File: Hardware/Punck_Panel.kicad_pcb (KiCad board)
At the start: 2 copper layers, 91.2 x 128.5 mm, 37 parts, among them J11 USB_B_Micro

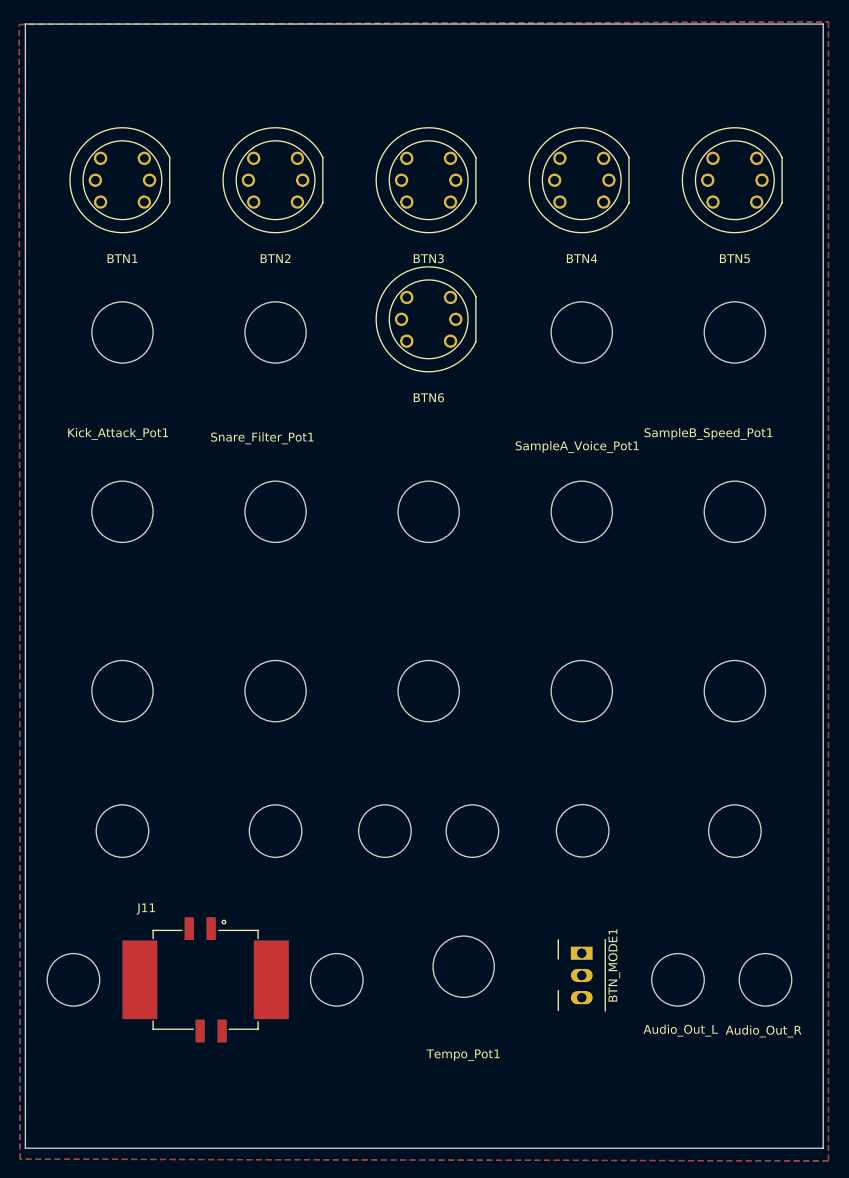
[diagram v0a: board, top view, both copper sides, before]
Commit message: Updated components on panel board
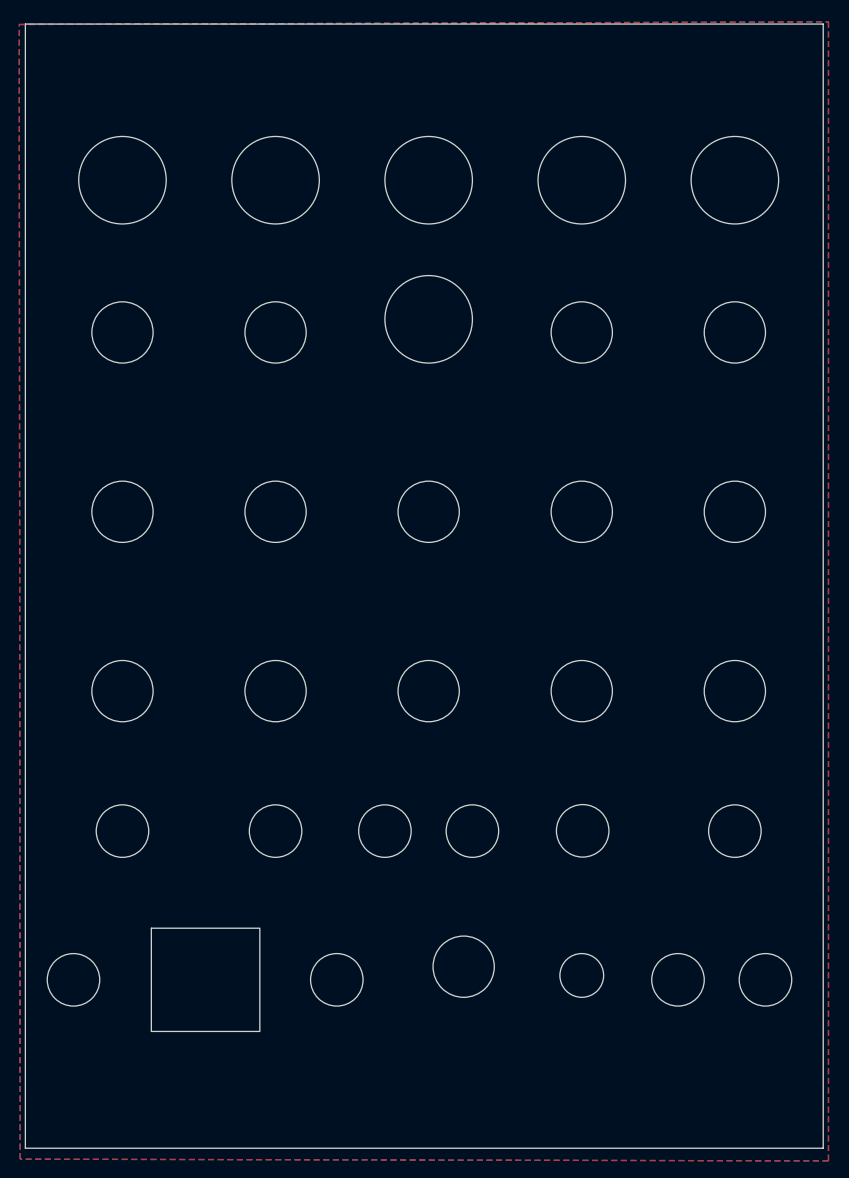
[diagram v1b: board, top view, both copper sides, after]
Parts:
- removed BTN1, BTN2, BTN3, BTN4, BTN5, BTN6: KS01-BLV, Custom_Footprints:KS01-BLV
- removed BTN_MODE1: SW_SPDT_MSM, Custom_Footprints:SPDT_SubMiniature_Aligned
- removed J11: USB_B_Micro, Custom_Footprints:USB_TE_1734517-1
- added Ref**: LED_Buttons_KS01-BLV, Custom_Footprints:LED_Buttons_KS01-BLV, F.Cu at (81.0, 58.6)
- added Ref**: LED_Buttons_KS01-BLV, Custom_Footprints:LED_Buttons_KS01-BLV, F.Cu at (116.0, 58.6)
- added Ref**: LED_Buttons_KS01-BLV, Custom_Footprints:LED_Buttons_KS01-BLV, F.Cu at (151.0, 58.6)
- added Ref**: LED_Buttons_KS01-BLV, Custom_Footprints:LED_Buttons_KS01-BLV, F.Cu at (133.5, 58.6)
- added Ref**: LED_Buttons_KS01-BLV, Custom_Footprints:LED_Buttons_KS01-BLV, F.Cu at (98.5, 58.6)
- added Ref**: LED_Buttons_KS01-BLV, Custom_Footprints:LED_Buttons_KS01-BLV, F.Cu at (116.0, 74.5)
- added Ref**: Subminiature_Switch, Custom_Footprints:Sub_Miniature_Switch_MountingHole_5mm, F.Cu at (133.5, 149.5)
- added USB**: USB_B_CUTOUT, Custom_Footprints:USB_B_CUTOUT, F.Cu at (90.5, 150.0)
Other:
- board text added: "Hi Hat Decay"
- board text added: "Hi Hat Level"
- board text added: "Kick Attack"
- board text added: "Kick Decay"
- board text added: "Kick Level"
- board text added: "MIDI In"
- board text added: "Out L"
- board text added: "Out R"
- board text added: "Sample A Level"
- board text added: "Sample A Speed"
- board text added: "Sample A Voice"
- board text added: "Sample B Level"
- board text added: "Sample B Speed"
- board text added: "Snare Filter"
- board text added: "Snare Level"
- board text added: "Snare Tuning"
- board text added: "Tempo"
- board text added: "Tempo Out"
- board text removed: "Audio_Out_L"
- board text removed: "Audio_Out_R"
- board text removed: "Kick_Attack_Pot1"
- board text removed: "SampleA_Voice_Pot1"
- board text removed: "SampleB_Speed_Pot1"
- board text removed: "Snare_Filter_Pot1"
- board text removed: "Tempo_Pot1"

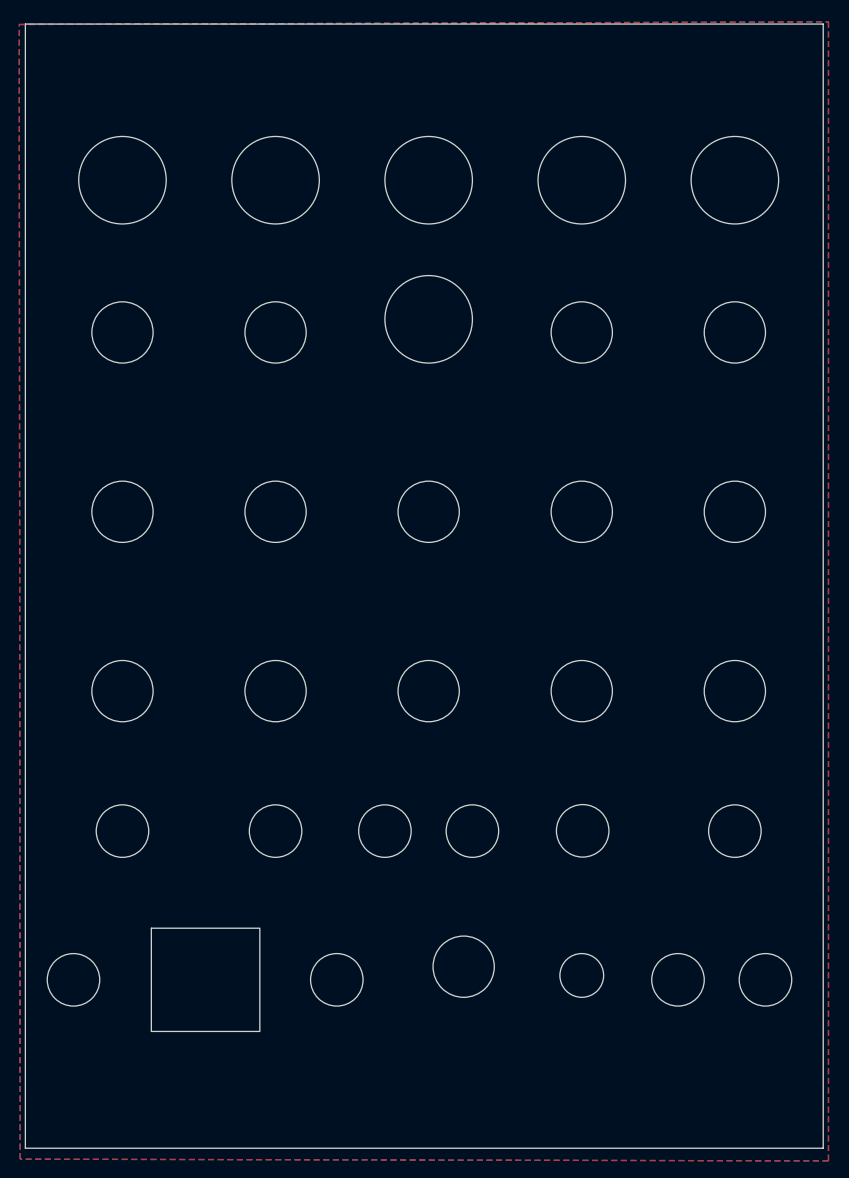
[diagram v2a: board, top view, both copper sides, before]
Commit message: Redesign of panel layout
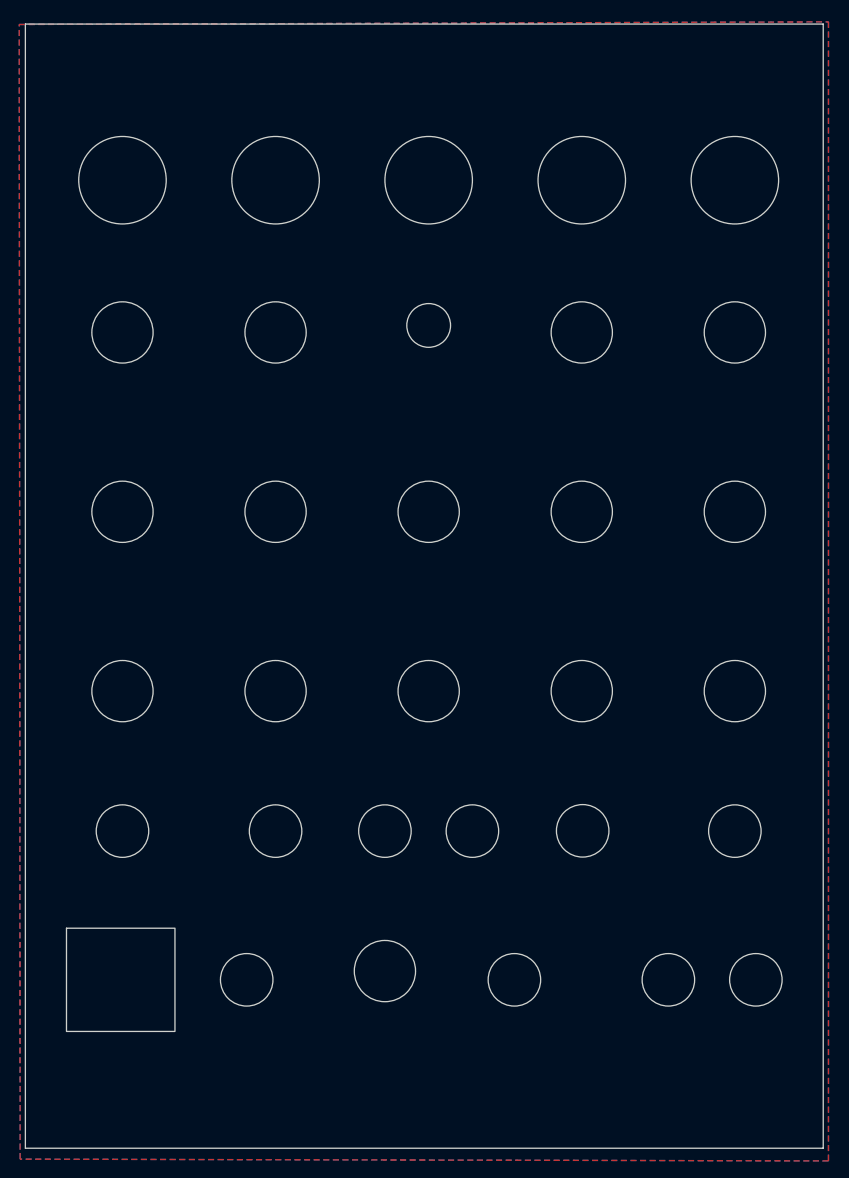
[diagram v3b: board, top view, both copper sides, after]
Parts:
- removed the Ref** at (116.0, 74.5)
- added kibuzzard-633EE0D0: G***, kibuzzard-633EE0D0, F.Cu at (81.2, 50.0)
- added kibuzzard-633EE0FA: G***, kibuzzard-633EE0FA, F.Cu at (98.6, 50.0)
- added kibuzzard-633EE108: G***, kibuzzard-633EE108, F.Cu at (116.2, 50.0)
- added kibuzzard-633EE168: G***, kibuzzard-633EE168, F.Cu at (141.8, 50.0)
- moved Ref** 76.3 mm to (116.0, 75.2)
- moved Ref** 20.3 mm to (125.8, 150.0)
- moved Ref** 19.8 mm to (95.2, 150.0)
- moved USB** 9.70 mm to (80.8, 150.0)
- moved Ref** 9.01 mm to (111.0, 149.0)
- moved Ref** 1.10 mm to (153.4, 150.0)
- moved Ref** 1.10 mm to (143.4, 150.0)
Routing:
- added copper zone on B.Cu, net (none)
- added copper zone on F.Cu, net (none)
- removed copper zone on B.Cu, net GND
- removed copper zone on F.Cu, net GND
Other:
- board text added: "Attack"
- board text added: "C"
- board text added: "Decay"
- board text added: "Filter"
- board text added: "IN"
- board text added: "L Out R"
- board text added: "Level"
- board text added: "MIDI"
- board text added: "MIDI Learn"
- board text added: "O"
- board text added: "Out"
- board text added: "Sequence"
- board text added: "Speed"
- board text added: "Tuning"
- board text added: "Voice"
- board text removed: "Hi Hat Decay"
- board text removed: "Hi Hat Level"
- board text removed: "Kick Attack"
- board text removed: "Kick Decay"
- board text removed: "Kick Level"
- board text removed: "MIDI In"
- board text removed: "Out L"
- board text removed: "Out R"
- board text removed: "Sample A Level"
- board text removed: "Sample A Speed"
- board text removed: "Sample A Voice"
- board text removed: "Sample B Level"
- board text removed: "Sample B Speed"
- board text removed: "Snare Filter"
- board text removed: "Snare Level"
- board text removed: "Snare Tuning"
- board text removed: "Tempo Out"

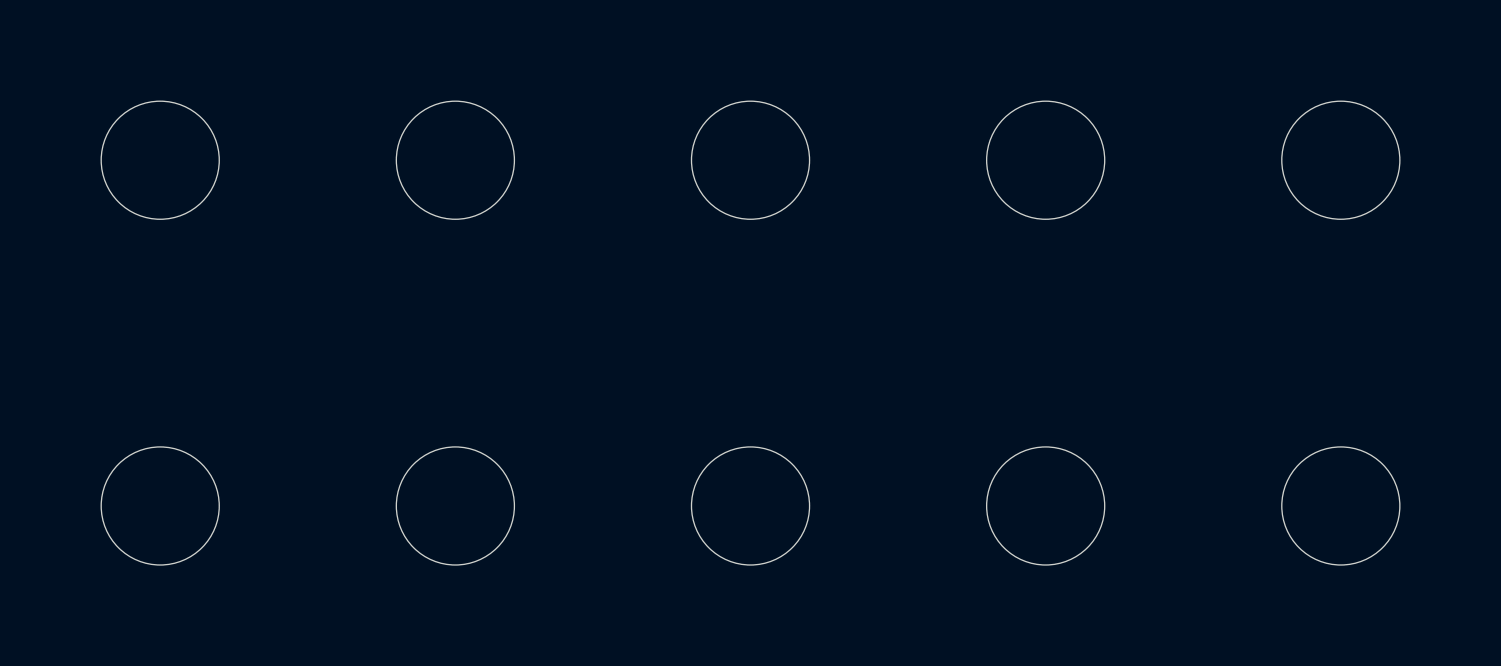
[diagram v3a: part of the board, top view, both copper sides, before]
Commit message: Updated PCBs to match changes in panel; ground returns improved
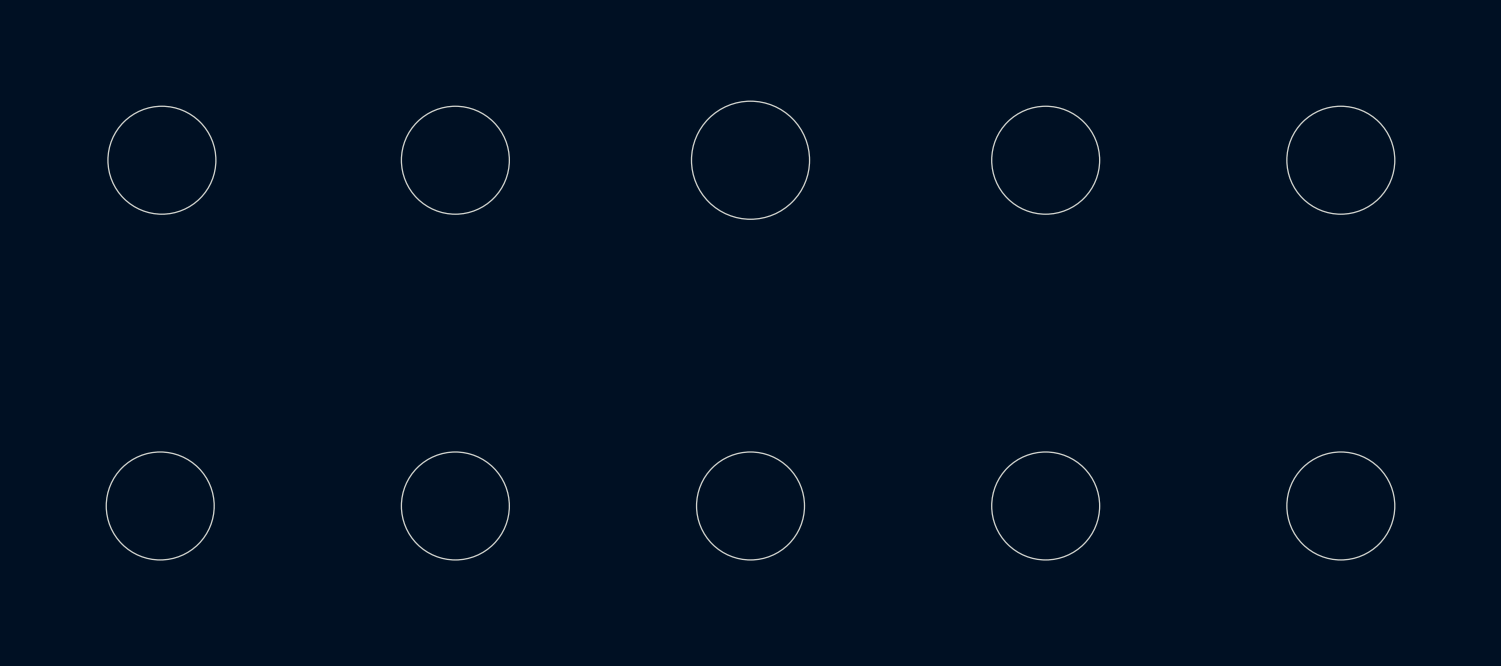
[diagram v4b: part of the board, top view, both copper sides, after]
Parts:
- removed the Ref** at (81.0, 96.5)
- removed kibuzzard-633EE108: G***, kibuzzard-633EE108
- added Ref**: Tall_Trimmer_Hole, Custom_Footprints:Tall_Trimmer_Hole, F.Cu at (81.1, 96.5)
- added kibuzzard-633EEB29: G***, kibuzzard-633EEB29, F.Cu at (116.2, 50.0)
- Ref** (x8): value Alpha_9mm_pot_hole -> Tall_Trimmer_Hole; footprint Custom_Footprints:Alpha_9mm_pot_hole -> Custom_Footprints:Tall_Trimmer_Hole
- moved kibuzzard-633EE0D0 0.20 mm to (81.0, 50.0)
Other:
- board text removed: "IN"

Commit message: More PCB tweaking
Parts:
- moved USB** 0.40 mm to (80.4, 150.0)
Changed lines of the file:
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@@
   )
   (footprint "Custom_Footprints:USB_B_CUTOUT" (layer "F.Cu")
-    (at 80.8 150)
+    (at 80.4 150)
     (attr smd)
     (fp_text reference "USB**" (at 0 -7 unlocked) (layer "F.SilkS") hide

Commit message: Added Logo to panel
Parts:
- added G***: LOGO, Graphics:punck, F.Cu at (116.0, 44.4)

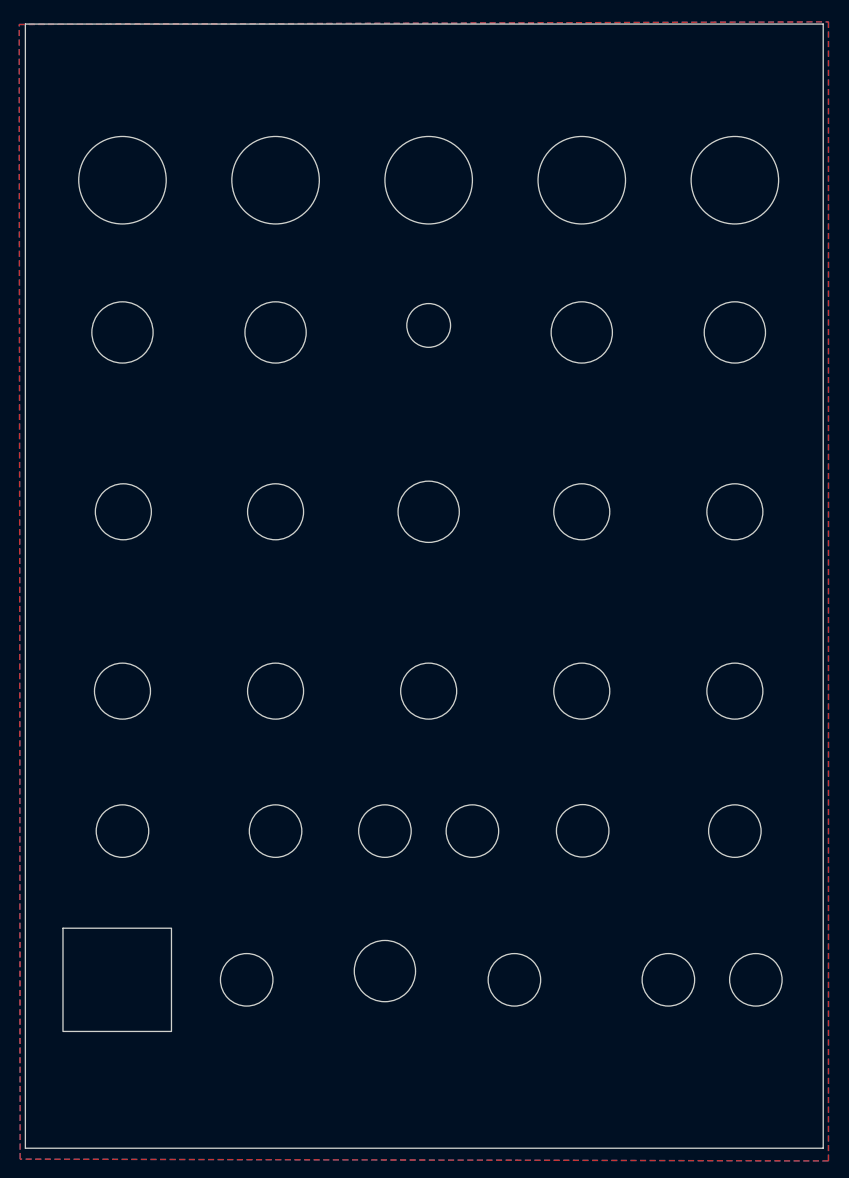
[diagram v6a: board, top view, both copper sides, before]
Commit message: More PCB tweaks; rejigged bottom row of controls
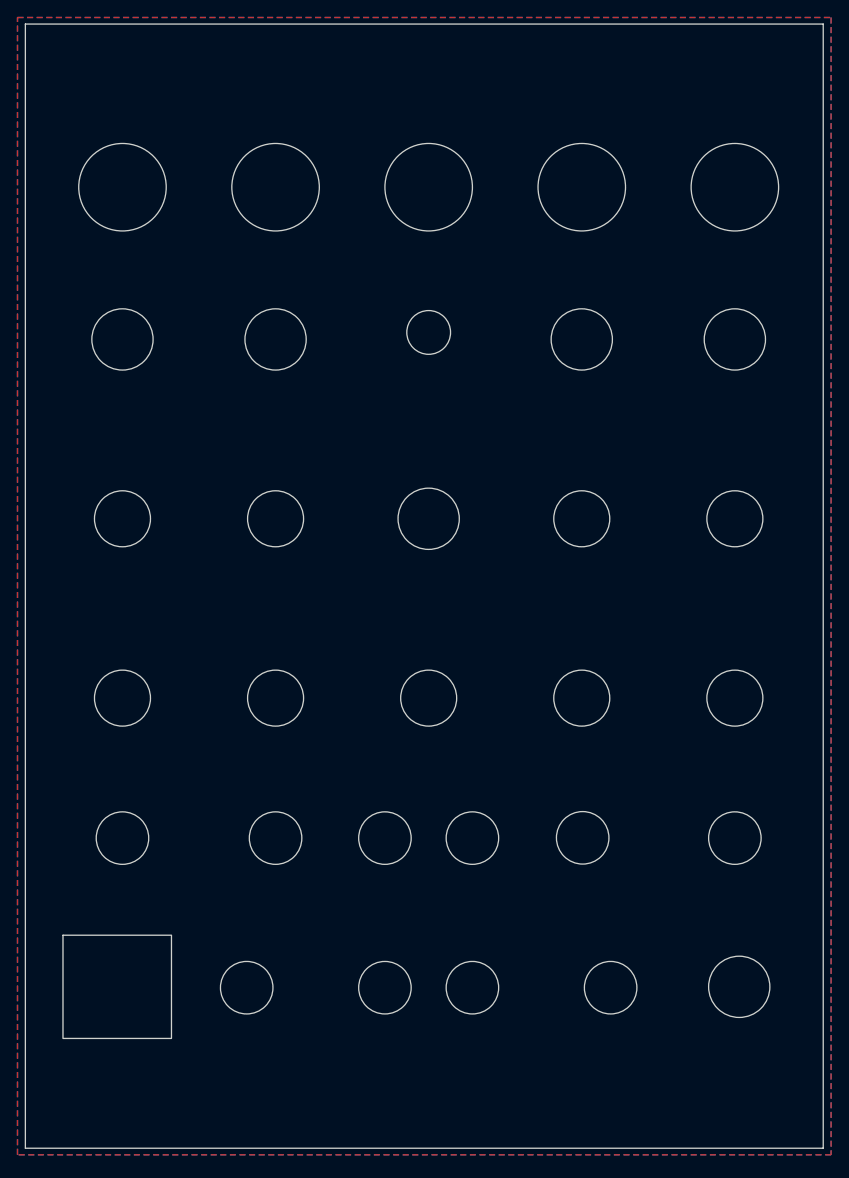
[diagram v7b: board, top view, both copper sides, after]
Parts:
- moved Ref** 40.5 mm to (151.5, 150.8)
- moved Ref** 32.4 mm to (121.0, 150.9)
- moved Ref** 32.4 mm to (111.0, 150.9)
- moved Ref** 11.0 mm to (136.8, 150.9)
- moved Ref** 0.90 mm to (95.2, 150.9)
- moved Ref** 0.81 mm to (81.0, 97.3)
- moved Ref** 0.80 mm to (133.6, 133.8)
- moved Ref** 0.80 mm to (98.5, 133.8)
- moved Ref** 0.80 mm to (81.0, 133.8)
- moved Ref** 0.80 mm to (121.0, 133.8)
- moved Ref** 0.80 mm to (151.0, 133.8)
- moved Ref** 0.80 mm to (111.0, 133.8)
- moved USB** 0.80 mm to (80.4, 150.8)
- moved Ref** 0.80 mm to (133.5, 97.3)
- moved Ref** 0.80 mm to (98.5, 117.8)
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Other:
- board text added: "Mountjoy Modular"
- board text added: "USB"
